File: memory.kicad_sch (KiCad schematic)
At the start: 3 parts, among them U5 M24C64-WMN6TP

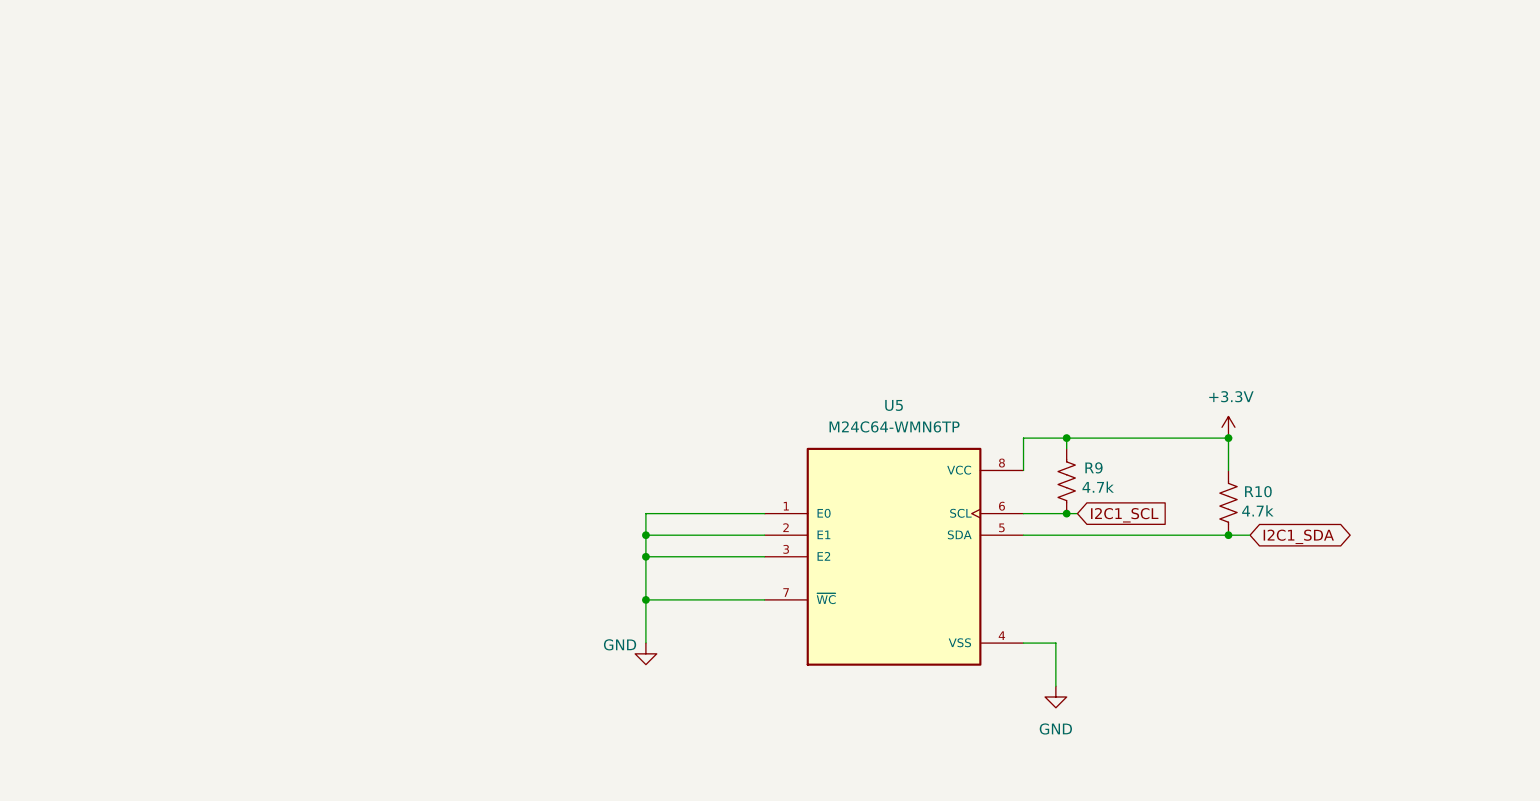
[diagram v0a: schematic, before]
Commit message: added memory and fixed clock
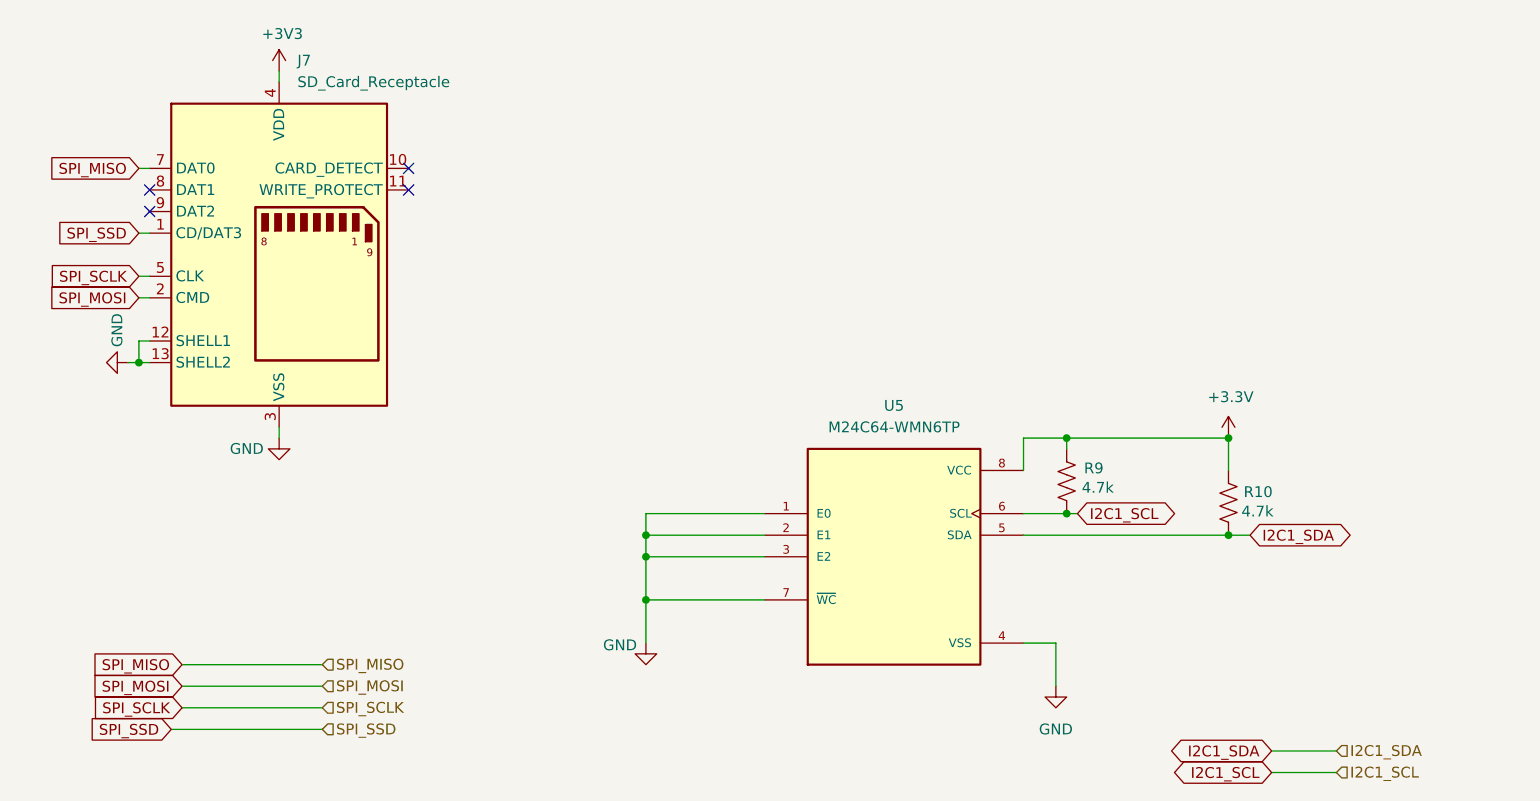
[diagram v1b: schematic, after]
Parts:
- added J7: SD_Card_Receptacle, Connector_Card:SD_Kyocera_145638009211859+, symbol Connector:SD_Card_Receptacle
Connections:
- net GND: now also J7.12 (SHELL1), J7.13 (SHELL2), J7.3 (VSS), J7.6 (VSS)
- new net +3V3: J7.4 (VDD)
- new net SPI_MISO: J7.7 (DAT0)
- new net SPI_MOSI: J7.2 (CMD)
- new net SPI_SCLK: J7.5 (CLK)
- new net SPI_SSD: J7.1 (CD/DAT3)
- no-connect marks 0 -> 4

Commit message: Updated Schematic
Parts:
- added C38: 100nF, symbol Device:C
- added U9: WE-TVS-824015043, Package_TO_SOT_SMD:SOT-23-6, symbol Power_Protection:WE-TVS-824015043
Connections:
- net +3.3V: now also C38.1
- net +3V3: now also U9.5 (VBUS)
- net GND: now also C38.2, U9.2 (GND)
- net SPI_MISO: now also U9.1 (I/O1)
- net SPI_MOSI: now also U9.6 (I/O4)
- net SPI_SCLK: now also U9.4 (I/O3)
- net SPI_SSD: now also U9.3 (I/O2)

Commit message: Updated Audio with ESD Diode
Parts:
- C38: footprint (none) -> Capacitor_SMD:C_0805_2012Metric
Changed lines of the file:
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@@
 			)
 		)
-		(property "Footprint" ""
+		(property "Footprint" "Capacitor_SMD:C_0805_2012Metric"
 			(at 207.9752 102.87 0)
 			(effects

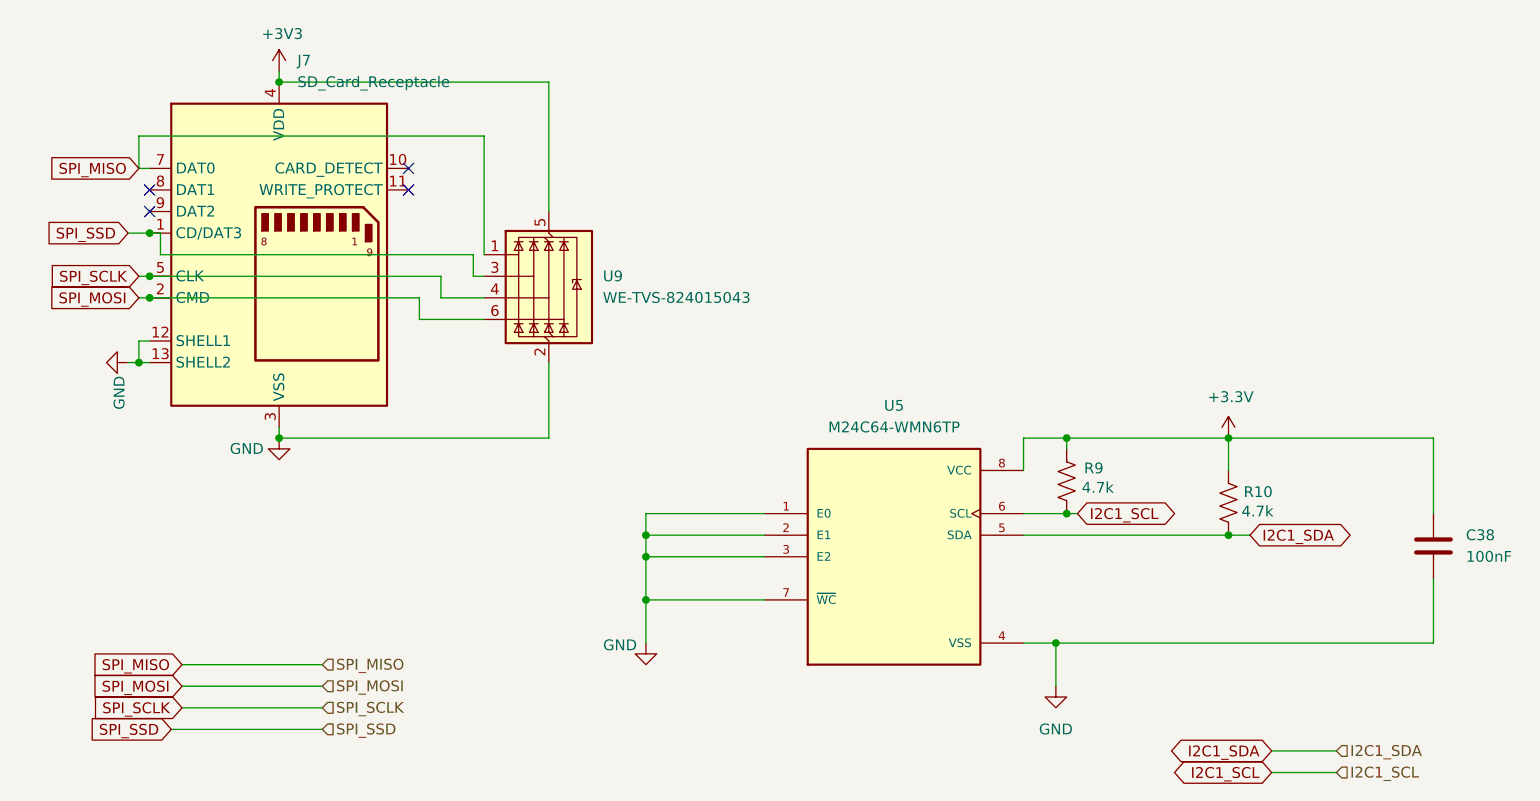
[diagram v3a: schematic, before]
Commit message: Fixed labels and added datasheets
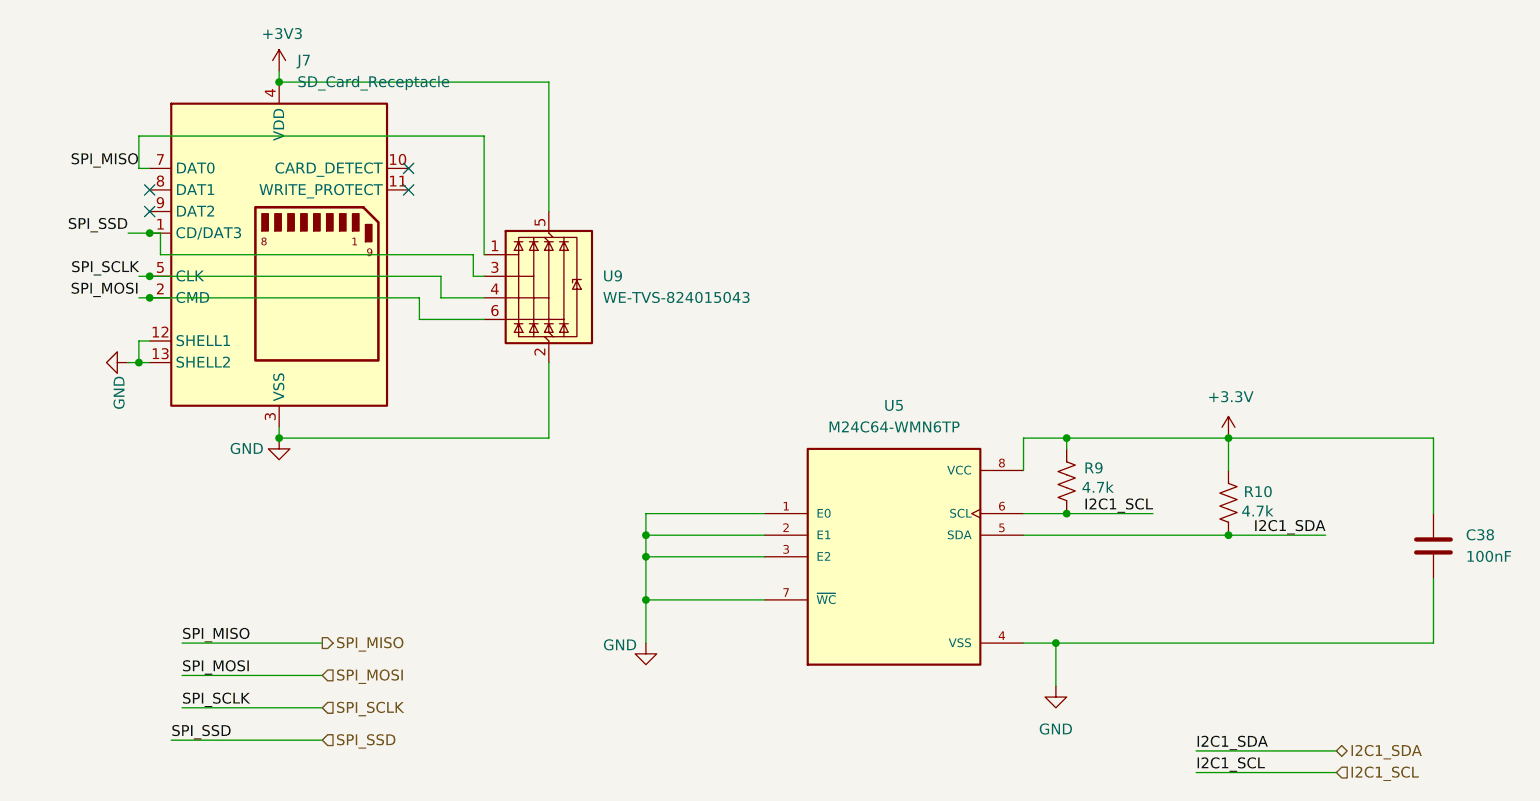
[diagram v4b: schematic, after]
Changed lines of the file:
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@@
+	(wire
+		(pts
+			(xy 179.07 125.73) (xy 195.58 125.73)
+		)
+		(stroke
+			(width 0)
+			(type default)
+		)
+	)
 	(wire
 		(pts
@@
 	(wire
 		(pts
-			(xy 182.88 97.79) (xy 185.42 97.79)
+			(xy 182.88 97.79) (xy 194.31 97.79)
 		)
 		(stroke
@@
 	(wire
 		(pts
-			(xy 187.96 123.19) (xy 195.58 123.19)
-		)
-		(stroke
-			(width 0)
-			(type default)
-		)
-	)
-	(wire
-		(pts
-			(xy 59.69 115.57) (xy 76.2 115.57)
+			(xy 59.69 114.3) (xy 76.2 114.3)
 		)
 		(stroke
@@
 	(wire
 		(pts
-			(xy 59.69 113.03) (xy 76.2 113.03)
+			(xy 59.69 110.49) (xy 76.2 110.49)
 		)
 		(stroke
@@
 	(wire
 		(pts
-			(xy 163.83 95.25) (xy 165.1 95.25)
+			(xy 163.83 95.25) (xy 173.99 95.25)
 		)
 		(stroke
@@
 	(wire
 		(pts
-			(xy 58.42 120.65) (xy 76.2 120.65)
+			(xy 58.42 121.92) (xy 76.2 121.92)
 		)
 		(stroke
@@
 	(wire
 		(pts
-			(xy 187.96 125.73) (xy 195.58 125.73)
-		)
-		(stroke
-			(width 0)
-			(type default)
-		)
-	)
-	(wire
-		(pts
 			(xy 87.63 72.39) (xy 95.25 72.39)
 		)
@@
 	(wire
 		(pts
+			(xy 179.07 123.19) (xy 195.58 123.19)
+		)
+		(stroke
+			(width 0)
+			(type default)
+		)
+	)
+	(wire
+		(pts
 			(xy 59.69 118.11) (xy 76.2 118.11)
 		)
@@
 		)
 	)
-	(global_label "I2C1_SCL"
-		(shape bidirectional)
-		(at 187.96 125.73 180)
-		(fields_autoplaced yes)
-		(effects
-			(font
-				(size 1.27 1.27)
-			)
-			(justify right)
-		)
-		(property "Intersheetrefs" "${INTERSHEET_REFS}"
-			(at 175.0945 125.73 0)
-			(effects
-				(font
-					(size 1.27 1.27)
-				)
-				(justify right)
-				(hide yes)
-			)
-		)
-	)
-	(global_label "I2C1_SDA"
-		(shape bidirectional)
-		(at 185.42 97.79 0)
-		(fields_autoplaced yes)
-		(effects
-			(font
-				(size 1.27 1.27)
-			)
-			(justify left)
-		)
-		(property "Intersheetrefs" "${INTERSHEET_REFS}"
-			(at 198.346 97.79 0)
-			(effects
-				(font
-					(size 1.27 1.27)
-				)
-				(justify left)
-				(hide yes)
-			)
-		)
-	)
-	(global_label "SPI_MISO"
-		(shape input)
-		(at 59.69 113.03 180)
-		(fields_autoplaced yes)
-		(effects
-			(font
-				(size 1.27 1.27)
-			)
-			(justify right)
-		)
-		(property "Intersheetrefs" "${INTERSHEET_REFS}"
-			(at 48.0567 113.03 0)
-			(effects
-				(font
-					(size 1.27 1.27)
-				)
-				(justify right)
-				(hide yes)
-			)
-		)
-	)
-	(global_label "I2C1_SDA"
-		(shape bidirectional)
-		(at 187.96 123.19 180)
-		(fields_autoplaced yes)
-		(effects
-			(font
-				(size 1.27 1.27)
-			)
-			(justify right)
-		)
-		(property "Intersheetrefs" "${INTERSHEET_REFS}"
-			(at 175.034 123.19 0)
-			(effects
-				(font
-					(size 1.27 1.27)
-				)
-				(justify right)
-				(hide yes)
-			)
-		)
-	)
-	(global_label "SPI_MOSI"
-		(shape input)
+	(label "I2C1_SDA"
+		(at 179.07 123.19 0)
+		(effects
+			(font
+				(size 1.27 1.27)
+			)
+			(justify left bottom)
+		)
+	)
+	(label "SPI_SSD"
+		(at 53.34 62.23 180)
+		(effects
+			(font
+				(size 1.27 1.27)
+			)
+			(justify right bottom)
+		)
+	)
+	(label "I2C1_SCL"
+		(at 179.07 125.73 0)
+		(effects
+			(font
+				(size 1.27 1.27)
+			)
+			(justify left bottom)
+		)
+	)
+	(label "SPI_MISO"
+		(at 54.61 54.61 180)
+		(effects
+			(font
+				(size 1.27 1.27)
+			)
+			(justify right bottom)
+		)
+	)
+	(label "SPI_SCLK"
+		(at 59.69 118.11 0)
+		(effects
+			(font
+				(size 1.27 1.27)
+			)
+			(justify left bottom)
+		)
+	)
+	(label "SPI_SCLK"
+		(at 54.61 67.31 180)
+		(effects
+			(font
+				(size 1.27 1.27)
+			)
+			(justify right bottom)
+		)
+	)
+	(label "I2C1_SDA"
+		(at 194.31 97.79 180)
+		(effects
+			(font
+				(size 1.27 1.27)
+			)
+			(justify right bottom)
+		)
+	)
+	(label "SPI_SSD"
+		(at 58.42 121.92 0)
+		(effects
+			(font
+				(size 1.27 1.27)
+			)
+			(justify left bottom)
+		)
+	)
+	(label "SPI_MOSI"
+		(at 59.69 114.3 0)
+		(effects
+			(font
+				(size 1.27 1.27)
+			)
+			(justify left bottom)
+		)
+	)
+	(label "SPI_MISO"
+		(at 59.69 110.49 0)
+		(effects
+			(font
+				(size 1.27 1.27)
+			)
+			(justify left bottom)
+		)
+	)
+	(label "I2C1_SCL"
+		(at 173.99 95.25 180)
+		(effects
+			(font
+				(size 1.27 1.27)
+			)
+			(justify right bottom)
+		)
+	)
+	(label "SPI_MOSI"
 		(at 54.61 69.85 180)
-		(fields_autoplaced yes)
-		(effects
-			(font
-				(size 1.27 1.27)
-			)
-			(justify right)
-		)
-		(property "Intersheetrefs" "${INTERSHEET_REFS}"
-			(at 42.9767 69.85 0)
-			(effects
-				(font
-					(size 1.27 1.27)
-				)
-				(justify right)
-				(hide yes)
-			)
-		)
-	)
-	(global_label "I2C1_SCL"
-		(shape bidirectional)
-		(at 165.1 95.25 0)
-		(fields_autoplaced yes)
-		(effects
-			(font
-				(size 1.27 1.27)
-			)
-			(justify left)
-		)
-		(property "Intersheetrefs" "${INTERSHEET_REFS}"
-			(at 177.9655 95.25 0)
-			(effects
-				(font
-					(size 1.27 1.27)
-				)
-				(justify left)
-				(hide yes)
-			)
-		)
-	)
-	(global_label "SPI_SCLK"
-		(shape input)
-		(at 54.61 67.31 180)
-		(fields_autoplaced yes)
-		(effects
-			(font
-				(size 1.27 1.27)
-			)
-			(justify right)
-		)
-		(property "Intersheetrefs" "${INTERSHEET_REFS}"
-			(at 42.7953 67.31 0)
-			(effects
-				(font
-					(size 1.27 1.27)
-				)
-				(justify right)
-				(hide yes)
-			)
-		)
-	)
-	(global_label "SPI_SSD"
-		(shape input)
-		(at 53.34 62.23 180)
-		(fields_autoplaced yes)
-		(effects
-			(font
-				(size 1.27 1.27)
-			)
-			(justify right)
-		)
-		(property "Intersheetrefs" "${INTERSHEET_REFS}"
-			(at 42.6139 62.23 0)
-			(effects
-				(font
-					(size 1.27 1.27)
-				)
-				(justify right)
-				(hide yes)
-			)
-		)
-	)
-	(global_label "SPI_SSD"
-		(shape input)
-		(at 58.42 120.65 180)
-		(fields_autoplaced yes)
-		(effects
-			(font
-				(size 1.27 1.27)
-			)
-			(justify right)
-		)
-		(property "Intersheetrefs" "${INTERSHEET_REFS}"
-			(at 47.6939 120.65 0)
-			(effects
-				(font
-					(size 1.27 1.27)
-				)
-				(justify right)
-				(hide yes)
-			)
-		)
-	)
-	(global_label "SPI_SCLK"
-		(shape input)
-		(at 59.69 118.11 180)
-		(fields_autoplaced yes)
-		(effects
-			(font
-				(size 1.27 1.27)
-			)
-			(justify right)
-		)
-		(property "Intersheetrefs" "${INTERSHEET_REFS}"
-			(at 47.8753 118.11 0)
-			(effects
-				(font
-					(size 1.27 1.27)
-				)
-				(justify right)
-				(hide yes)
-			)
-		)
-	)
-	(global_label "SPI_MOSI"
-		(shape input)
-		(at 59.69 115.57 180)
-		(fields_autoplaced yes)
-		(effects
-			(font
-				(size 1.27 1.27)
-			)
-			(justify right)
-		)
-		(property "Intersheetrefs" "${INTERSHEET_REFS}"
-			(at 48.0567 115.57 0)
-			(effects
-				(font
-					(size 1.27 1.27)
-				)
-				(justify right)
-				(hide yes)
-			)
-		)
-	)
-	(global_label "SPI_MISO"
-		(shape input)
-		(at 54.61 54.61 180)
-		(fields_autoplaced yes)
-		(effects
-			(font
-				(size 1.27 1.27)
-			)
-			(justify right)
-		)
-		(property "Intersheetrefs" "${INTERSHEET_REFS}"
-			(at 42.9767 54.61 0)
-			(effects
-				(font
-					(size 1.27 1.27)
-				)
-				(justify right)
-				(hide yes)
-			)
+		(effects
+			(font
+				(size 1.27 1.27)
+			)
+			(justify right bottom)
 		)
 	)
@@
 	)
 	(hierarchical_label "SPI_MISO"
-		(shape input)
-		(at 76.2 113.03 0)
+		(shape output)
+		(at 76.2 110.49 0)
 		(effects
 			(font
@@
 	)
 	(hierarchical_label "I2C1_SDA"
-		(shape input)
+		(shape bidirectional)
 		(at 195.58 123.19 0)
 		(effects
@@
 	(hierarchical_label "SPI_MOSI"
 		(shape input)
-		(at 76.2 115.57 0)
+		(at 76.2 114.3 0)
 		(effects
 			(font
@@
 	(hierarchical_label "SPI_SSD"
 		(shape input)
-		(at 76.2 120.65 0)
-		(effects
-			(font
+		(at 76.2 121.92 0)
+		(effects
+			(font

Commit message: fixed some of the problems
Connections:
- net +3V3 is gone; now on net +3.3V: J7.4 (VDD), U9.5 (VBUS)
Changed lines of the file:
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@@
-	)
-	(symbol
-		(lib_id "power:+3V3")
-		(at 71.12 43.18 0)
-		(unit 1)
-		(exclude_from_sim no)
-		(in_bom yes)
-		(on_board yes)
-		(dnp no)
-		(property "Reference" "#PWR074"
-			(at 71.12 46.99 0)
-			(effects
-				(font
-					(size 1.27 1.27)
-				)
-				(hide yes)
-			)
-		)
-		(property "Value" "+3V3"
-			(at 71.501 38.7858 0)
-			(effects
-				(font
-					(size 1.27 1.27)
-				)
-			)
-		)
-		(property "Footprint" ""
-			(at 71.12 43.18 0)
-			(effects
-				(font
-					(size 1.27 1.27)
-				)
-				(hide yes)
-			)
-		)
-		(property "Datasheet" ""
-			(at 71.12 43.18 0)
-			(effects
-				(font
-					(size 1.27 1.27)
-				)
-				(hide yes)
-			)
-		)
-		(property "Description" ""
-			(at 71.12 43.18 0)
-			(effects
-				(font
-					(size 1.27 1.27)
-				)
-			)
-		)
-		(pin "1"
-		)
-		(instances
-			(project "senior_design"
-				(path "/35c074f0-8545-4dc1-a57d-3ef0bc7d9188/97e7f441-78af-47c4-8e49-e87c6db6b63d"
-					(reference "#PWR074")
-					(unit 1)
-				)
-			)
-		)
 	)
 	(symbol
@@
 					(unit 1)
 				)
+			)
+		)
+	)
+	(symbol
+		(lib_id "power:+3.3V")
+		(at 71.12 43.18 0)
+		(unit 1)
+		(exclude_from_sim no)
+		(in_bom yes)
+		(on_board yes)
+		(dnp no)
+		(fields_autoplaced yes)
+		(property "Reference" "#PWR042"
+			(at 71.12 46.99 0)
+			(effects
+				(font
+					(size 1.27 1.27)
+				)
+				(hide yes)
+			)
+		)
+		(property "Value" "+3.3V"
+			(at 71.12 38.1 0)
+			(effects
+				(font
+					(size 1.27 1.27)
+				)
+			)
+		)
+		(property "Footprint" ""
+			(at 71.12 43.18 0)
+			(effects
+				(font
+					(size 1.27 1.27)
+				)
+				(hide yes)
+			)
+		)
+		(property "Datasheet" ""
+			(at 71.12 43.18 0)
+			(effects
+				(font
+					(size 1.27 1.27)
+				)
+				(hide yes)
+			)
+		)
+		(property "Description" "Power symbol creates a global label with name \"+3.3V\""
+			(at 71.12 43.18 0)
+			(effects
+				(font
+					(size 1.27 1.27)
+				)
+				(hide yes)
+			)
+		)
+		(pin "1"
+		)
+		(instances
+			(project ""
+				(path "/35c074f0-8545-4dc1-a57d-3ef0bc7d9188/97e7f441-78af-47c4-8e49-e87c6db6b63d"
+					(reference "#PWR042")
+					(unit 1)
+				)

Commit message: plane and jumper fix
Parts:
- removed U9: WE-TVS-824015043, Package_TO_SOT_SMD:SOT-23-6, symbol Power_Protection:WE-TVS-824015043
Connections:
- no-connect marks 4 -> 2
